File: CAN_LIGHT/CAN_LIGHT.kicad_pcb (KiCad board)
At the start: 2 copper layers, 135.5 x 115.4 mm, 93 parts, among them J1 Conn_ARM_SWD_TagConnect_TC2030

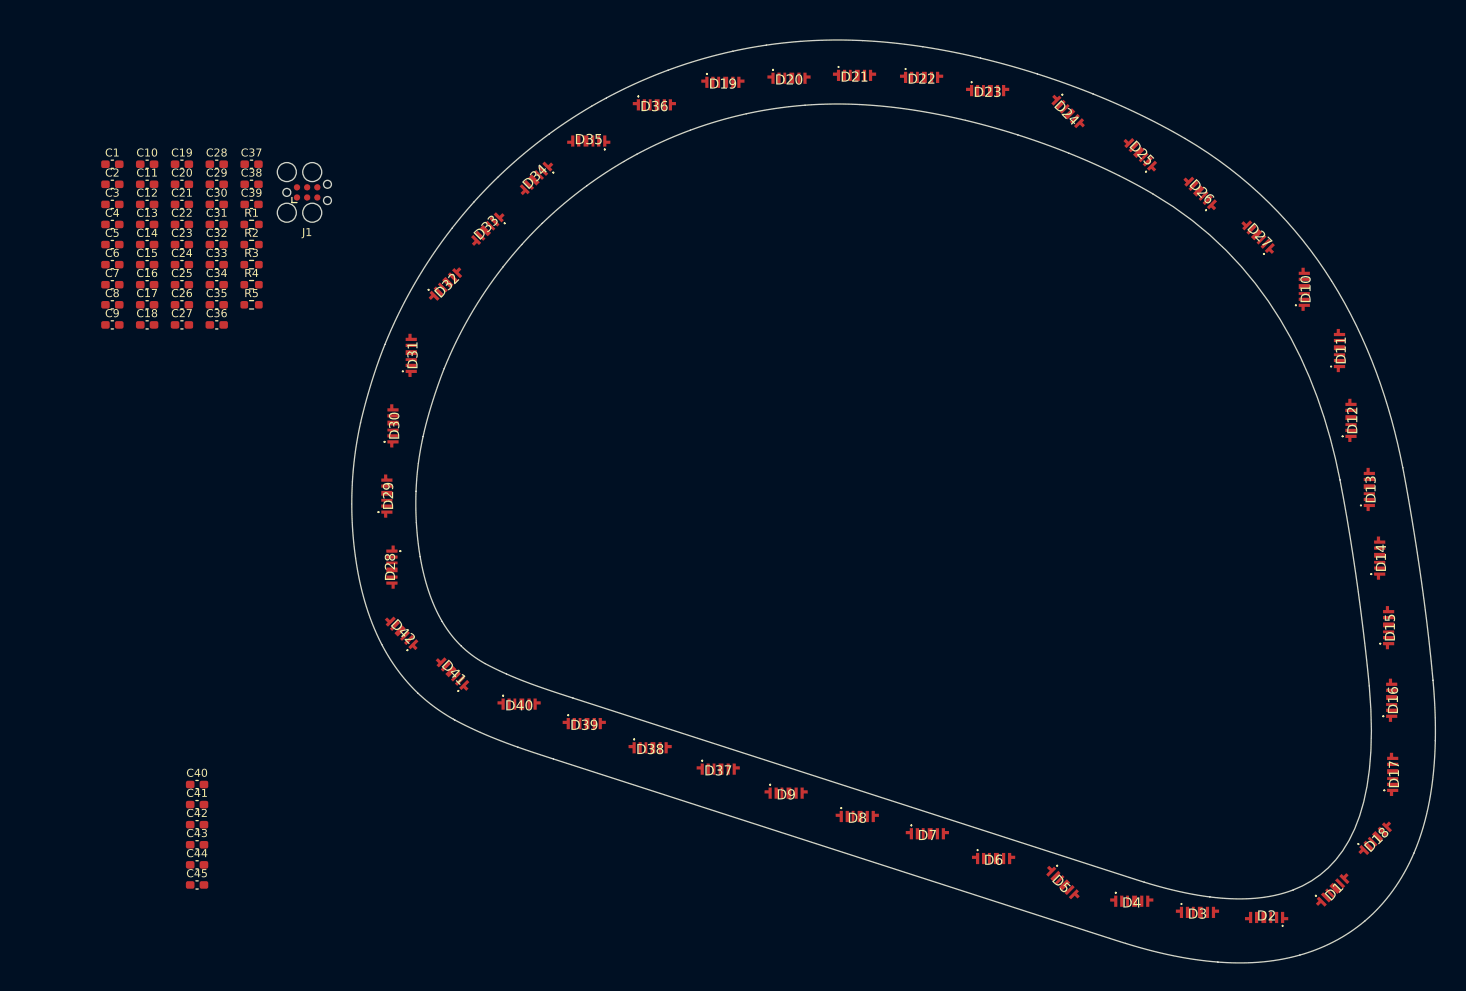
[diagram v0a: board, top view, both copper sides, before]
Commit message: Place more LEDs and experiment with routing paths
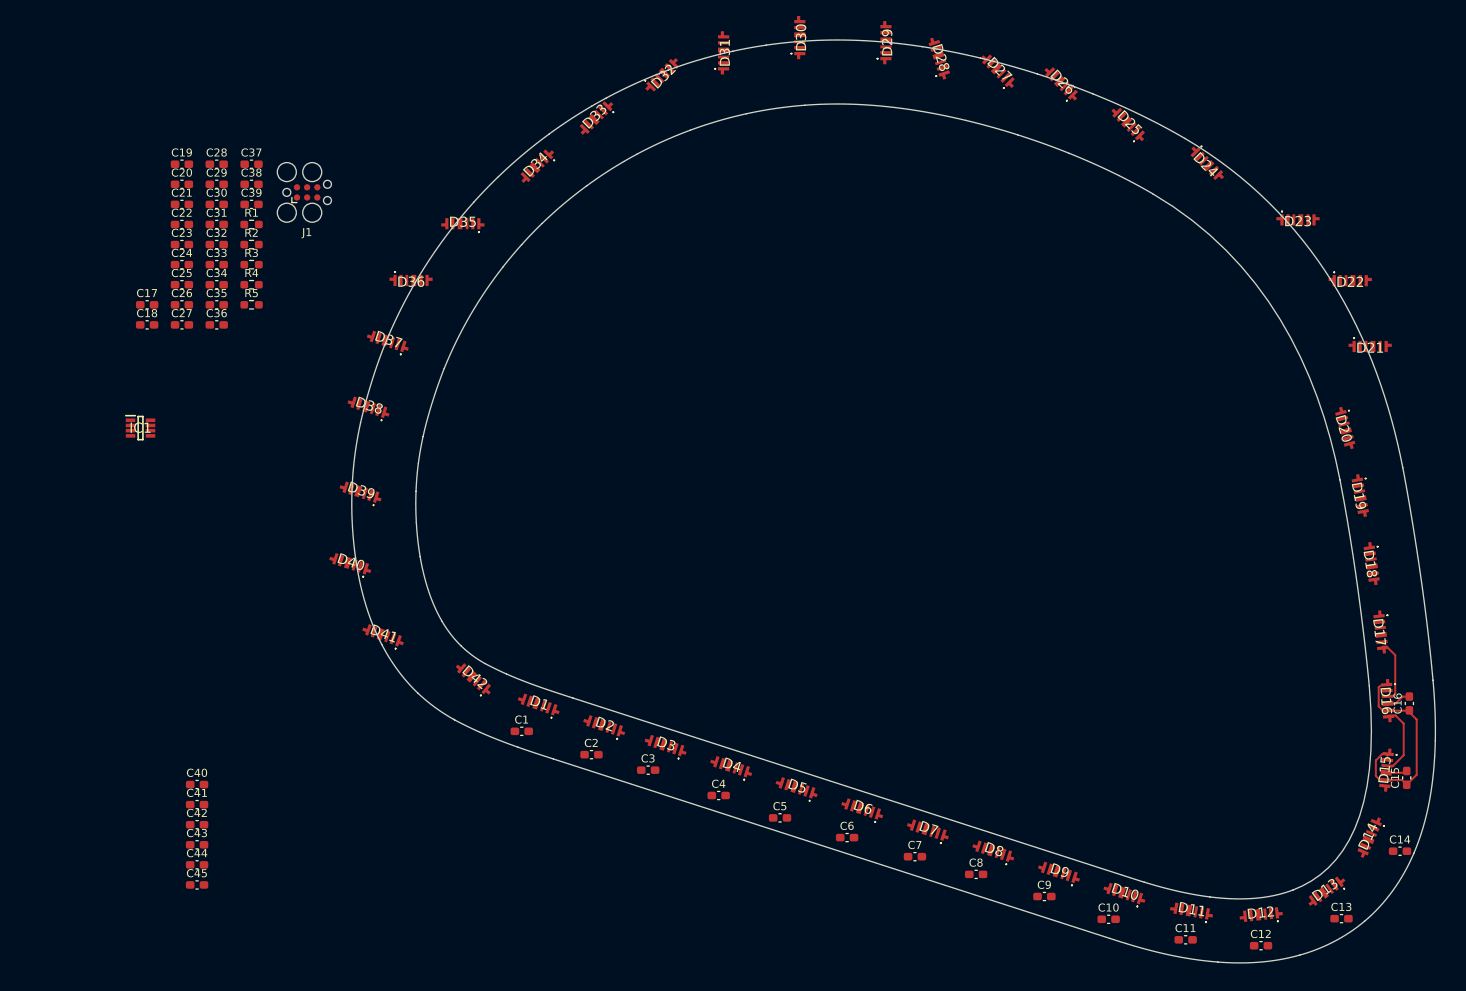
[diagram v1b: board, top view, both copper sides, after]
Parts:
- added IC1: MSPM0C1103SDDFR, MSPM0C1103SDDFR:SOT65P280X110-8N, F.Cu at (39.6, 76.2)
- C1: value 10uF -> 0.1uF
- C3: value 10nF -> 0.1uF
- C43: value 0.1uF -> 10uF
- C45: value 0.1uF -> 10nF
- R4: value 301K -> 169K
- R5: value 169K -> 301K
- moved C14 174.0 mm to (197.0, 129.1)
- moved C13 172.7 mm to (189.7, 137.6)
- moved C15 170.0 mm to (197.8, 120.0), turned to 90 degrees
- moved C12 167.3 mm to (179.6, 140.9)
- moved C16 166.2 mm to (198.2, 110.7), turned to 90 degrees
- moved C11 160.5 mm to (170.2, 140.2)
- moved C10 152.8 mm to (160.6, 137.6)
- moved C9 136.7 mm to (152.6, 134.8)
- moved C8 129.3 mm to (144.0, 132.0)
- moved C7 123.2 mm to (136.4, 129.8)
- moved C6 116.5 mm to (127.9, 127.4)
- moved C5 110.0 mm to (119.5, 125.0)
- moved C4 104.1 mm to (111.8, 122.2)
- moved D1 102.2 mm to (89.5, 110.5), turned to 161 degrees
- moved C3 97.4 mm to (103.0, 119.0)
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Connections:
- C1 pad 1: +3.3V -> +5V
- C2 pad 1: +3.3V -> +5V
- C3 pad 1: Net-(IC1-PA1_/_NRST) -> +5V
- C43 pad 1: +5V -> +3.3V
- C44 pad 1: +5V -> +3.3V
- C45 pad 1: +5V -> Net-(IC1-PA1_/_NRST)
- D11 pad 6: Net-(D11-DIN) -> Net-(D10-DOUT)
- D20 pad 6: Net-(D20-DIN) -> Net-(D19-DOUT)
- D21 pad 6: Net-(D21-DIN) -> Net-(D20-DOUT)
- D22 pad 6: Net-(D19-DOUT) -> Net-(D21-DOUT)
- D23 pad 6: Net-(D20-DOUT) -> Net-(D22-DOUT)
- D24 pad 6: Net-(D21-DOUT) -> Net-(D23-DOUT)
- D25 pad 6: Net-(D22-DOUT) -> Net-(D24-DOUT)
- D26 pad 6: Net-(D23-DOUT) -> Net-(D25-DOUT)
- D27 pad 6: Net-(D24-DOUT) -> Net-(D26-DOUT)
- D28 pad 6: Net-(D25-DOUT) -> Net-(D27-DOUT)
- D29 pad 6: Net-(D26-DOUT) -> Net-(D28-DOUT)
- D30 pad 6: Net-(D27-DOUT) -> Net-(D29-DOUT)
- D31 pad 6: Net-(D28-DOUT) -> Net-(D30-DOUT)
- D32 pad 6: Net-(D29-DOUT) -> Net-(D31-DOUT)
- D33 pad 6: Net-(D30-DOUT) -> Net-(D32-DOUT)
- D34 pad 3: Net-(D20-DIN) -> Net-(D34-DOUT)
- D34 pad 6: Net-(D31-DOUT) -> Net-(D33-DOUT)
- D35 pad 3: Net-(D21-DIN) -> Net-(D35-DOUT)
- D35 pad 6: Net-(D32-DOUT) -> Net-(D34-DOUT)
- D36 pad 6: Net-(D33-DOUT) -> Net-(D35-DOUT)
- D5 pad 6: Net-(D10-DOUT) -> Net-(D4-DOUT)
- D8 pad 3: Net-(D11-DIN) -> Net-(D8-DOUT)
- D9 pad 6: Net-(D4-DOUT) -> Net-(D8-DOUT)
- R4 pad 2: +3.3V -> GND
- R5 pad 2: GND -> +3.3V
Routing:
- net +5V: track 0.00 -> 24.9 mm
- net Net-(D15-DOUT): track 0.00 -> 8.89 mm
- net Net-(D16-DOUT): track 0.00 -> 8.00 mm
- net GND: track 0.00 -> 5.71 mm

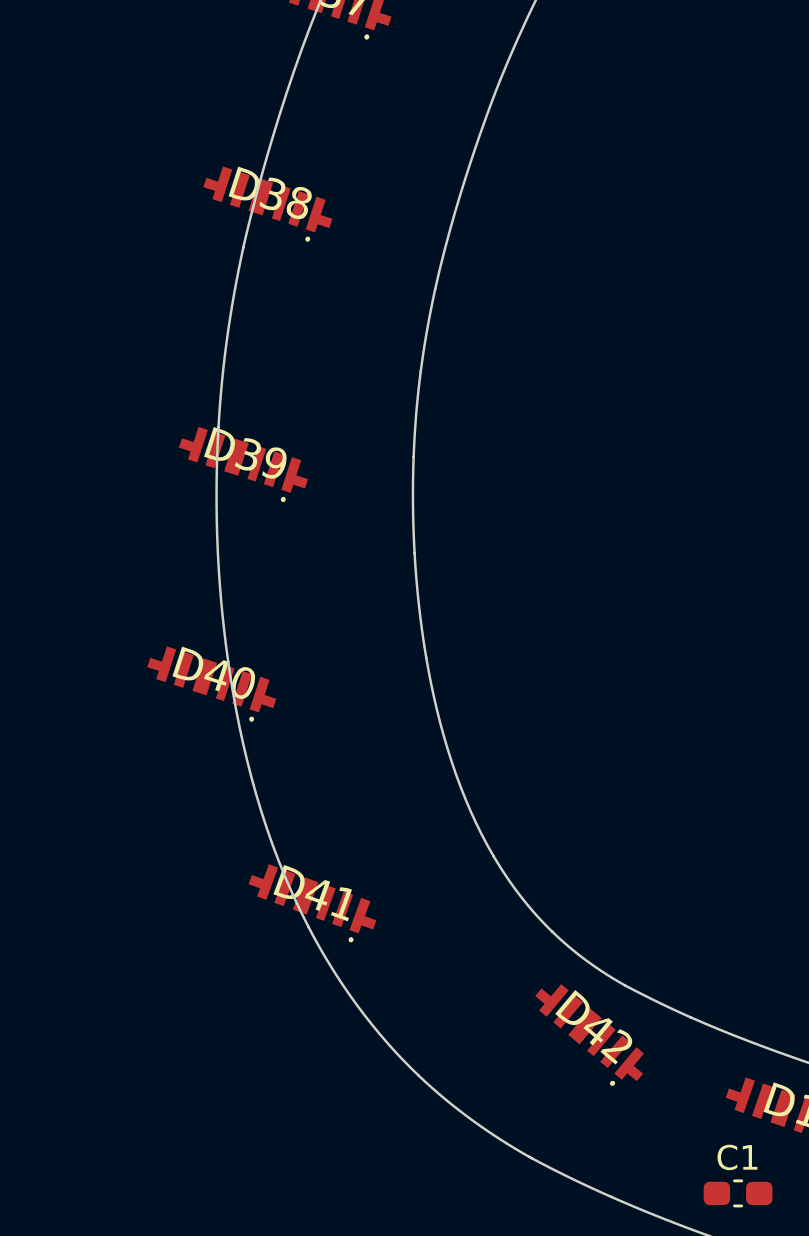
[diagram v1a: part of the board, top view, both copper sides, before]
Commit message: Place more LEDs
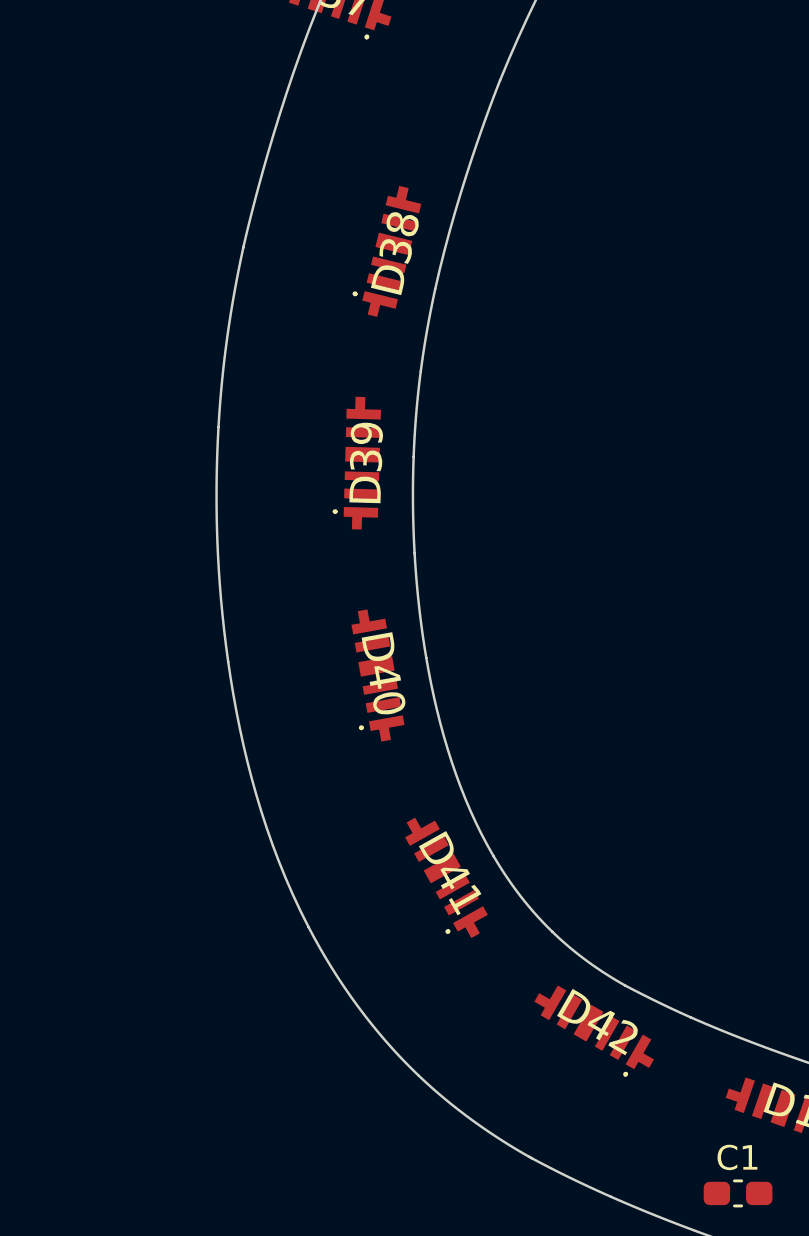
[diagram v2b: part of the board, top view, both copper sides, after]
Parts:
- moved D40 6.93 mm to (72.8, 93.0), turned to 100.25 degrees
- moved D38 5.77 mm to (73.4, 75.9), turned to 76.25 degrees
- moved D41 5.62 mm to (75.6, 101.1), turned to 119.25 degrees
- moved D39 5.02 mm to (72.2, 84.4), turned to 88.4 degrees
- moved D42 0.26 mm to (81.6, 107.1), turned to 150 degrees

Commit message: Finish LED placements
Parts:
- moved C17 163.3 mm to (198.7, 101.1)
- moved C18 159.9 mm to (197.6, 92.6)
- moved C19 157.0 mm to (196.5, 83.6)
- moved C20 153.4 mm to (195.4, 74.8)
- moved C21 148.9 mm to (192.6, 66.2)
- moved C22 143.0 mm to (187.6, 57.8)
- moved C23 136.5 mm to (181.3, 50.5)
- moved C24 130.2 mm to (174.5, 44.5)
- moved C25 122.9 mm to (166.1, 39.1)
- moved C26 115.6 mm to (157.7, 36.0)
- moved C27 108.9 mm to (149.4, 33.0)
- moved C28 91.9 mm to (140.2, 31.0)
- moved C29 83.5 mm to (131.1, 30.0)
- moved C30 74.6 mm to (121.3, 29.5)
- moved C31 65.1 mm to (111.4, 31.9)
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
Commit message: Place caps
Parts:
- moved C20 2.76 mm to (192.8, 75.7), turned to 105.75 degrees
- moved C21 2.75 mm to (190.0, 67.1), turned to 113.5 degrees
- moved C25 2.10 mm to (165.9, 41.1), turned to 152.5 degrees
- moved C34 2.06 mm to (88.9, 44.7), turned to -139.75 degrees
- moved C22 1.97 mm to (185.9, 58.9), turned to 122.75 degrees
- moved C19 1.97 mm to (194.8, 84.6), turned to 100.5 degrees
- moved C30 1.86 mm to (121.9, 31.2), turned to -175.5 degrees
- moved C35 1.83 mm to (82.8, 51.1), turned to -130.75 degrees
- moved C24 1.82 mm to (173.5, 46.0), turned to 143.5 degrees
- moved C36 1.81 mm to (77.2, 58.4), turned to -121.5 degrees
- moved C29 1.69 mm to (132.3, 31.2), turned to 175.5 degrees
- moved C5 1.65 mm to (120.1, 123.4), turned to -18 degrees
- moved C1 1.62 mm to (88.4, 113.0), turned to -19 degrees
- moved C23 1.58 mm to (180.1, 51.6), turned to 133 degrees
- moved C28 1.57 mm to (140.7, 32.5), turned to 168.6 degrees
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
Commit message: Mess with routing
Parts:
- moved C2 1.26 mm to (95.6, 115.4)
- moved C1 1.11 mm to (87.3, 112.7)
- moved C42 0.86 mm to (79.0, 108.8)
- moved C3 0.51 mm to (103.2, 117.8)
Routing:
- net +5V: track 24.9 -> 36.0 mm
- net GND: track 5.71 -> 16.6 mm
- net Net-(D1-DOUT): track 0.00 -> 8.23 mm
- net Net-(D2-DOUT): track 0.00 -> 7.06 mm
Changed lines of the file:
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@@
   )
   (footprint "Capacitor_SMD:C_0603_1608Metric_Pad1.08x0.95mm_HandSolder" (layer "F.Cu")
-    (at 96.774 115.824 -18)
+    (at 95.572714 115.430473 -18)
     (descr "Capacitor SMD 0603 (1608 Metric), square (rectangular) end terminal, IPC_7351 nominal with elongated pad for handsoldering. (Body size source: IPC-SM-782 page 76, https://www.pcb-3d.com/wordpress/wp-content/uploads/ipc-sm-782a_amendment_1_and_2.pdf), generated with kicad-footprint-generator")
     (tags "capacitor handsolder")
@@
   )
   (footprint "Capacitor_SMD:C_0603_1608Metric_Pad1.08x0.95mm_HandSolder" (layer "F.Cu")
-    (at 79.756 109.22 -30)
+    (at 79.009053 108.78875 -30)
     (descr "Capacitor SMD 0603 (1608 Metric), square (rectangular) end terminal, IPC_7351 nominal with elongated pad for handsoldering. (Body size source: IPC-SM-782 page 76, https://www.pcb-3d.com/wordpress/wp-content/uploads/ipc-sm-782a_amendment_1_and_2.pdf), generated with kicad-footprint-generator")
     (tags "capacitor handsolder")
@@
   )
   (footprint "Capacitor_SMD:C_0603_1608Metric_Pad1.08x0.95mm_HandSolder" (layer "F.Cu")
-    (at 103.632 118.11 -18)
+    (at 103.192714 117.843473 -18)
     (descr "Capacitor SMD 0603 (1608 Metric), square (rectangular) end terminal, IPC_7351 nominal with elongated pad for handsoldering. (Body size source: IPC-SM-782 page 76, https://www.pcb-3d.com/wordpress/wp-content/uploads/ipc-sm-782a_amendment_1_and_2.pdf), generated with kicad-footprint-generator")
     (tags "capacitor handsolder")
@@
   )
   (footprint "Capacitor_SMD:C_0603_1608Metric_Pad1.08x0.95mm_HandSolder" (layer "F.Cu")
-    (at 88.392 113.03 -19)
+    (at 87.32249 112.749197 -19)
     (descr "Capacitor SMD 0603 (1608 Metric), square (rectangular) end terminal, IPC_7351 nominal with elongated pad for handsoldering. (Body size source: IPC-SM-782 page 76, https://www.pcb-3d.com/wordpress/wp-content/uploads/ipc-sm-782a_amendment_1_and_2.pdf), generated with kicad-footprint-generator")
     (tags "capacitor handsolder")
@@
   (gr_curve (pts (xy 93.6303 109.9898) (xy 90.8143 109.0833) (xy 87.9942 108.1676) (xy 85.285899 106.9696))
     (stroke (width 0.1) (type solid)) (layer "Edge.Cuts"))
+  (segment (start 97.028 113.568986) (end 97.028 115.062) (width 0.25) (layer "F.Cu") (net 2))
+  (segment (start 87.884 112.776) (end 88.138 113.03) (width 0.25) (layer "F.Cu") (net 2))
+  (segment (start 87.884 112.014) (end 87.884 112.776) (width 0.25) (layer "F.Cu") (net 2))
+  (segment (start 104.908225 115.821761) (end 104.394 116.335986) (width 0.25) (layer "F.Cu") (net 2))
+  (segment (start 104.394 116.335986) (end 104.394 117.729) (width 0.25) (layer "F.Cu") (net 2))
   (segment (start 198.171067 109.806133) (end 197.330667 109.806133) (width 0.25) (layer "F.Cu") (net 2))
   (segment (start 195.282972 119.327641) (end 197.615758 119.327641) (width 0.25) (layer "F.Cu") (net 2))
+  (segment (start 81.131691 107.2062) (end 79.756 108.581891) (width 0.25) (layer "F.Cu") (net 2))
   (segment (start 197.615758 119.327641) (end 197.8406 119.102799) (width 0.25) (layer "F.Cu") (net 2))
   (segment (start 197.330667 109.806133) (end 196.468167 110.668633) (width 0.25) (layer "F.Cu") (net 2))
+  (segment (start 97.237425 113.359561) (end 97.028 113.568986) (width 0.25) (layer "F.Cu") (net 2))
   (segment (start 196.468167 110.668633) (end 195.469007 110.668633) (width 0.25) (layer "F.Cu") (net 2))
+  (segment (start 89.055598 110.685107) (end 89.055598 110.842402) (width 0.25) (layer "F.Cu") (net 2))
+  (segment (start 89.055598 110.842402) (end 87.884 112.014) (width 0.25) (layer "F.Cu") (net 2))
+  (segment (start 104.394 117.729) (end 104.013 118.11) (width 0.25) (layer "F.Cu") (net 2))
+  (segment (start 97.028 115.062) (end 96.393 115.697) (width 0.25) (layer "F.Cu") (net 2))
+  (segment (start 79.756 108.581891) (end 79.756 109.22) (width 0.25) (layer "F.Cu") (net 2))
   (segment (start 194.335426 108.661174) (end 194.335426 111.017225) (width 0.25) (layer "F.Cu") (net 4))
   (segment (start 195.244306 116.990515) (end 195.406986 117.153195) (width 0.25) (layer "F.Cu") (net 4))
+  (segment (start 96.381474 113.081446) (end 96.381474 113.5349) (width 0.25) (layer "F.Cu") (net 4))
+  (segment (start 104.052274 115.8971) (end 102.372428 117.576946) (width 0.25) (layer "F.Cu") (net 4))
   (segment (start 197.976654 111.566954) (end 195.523951 111.566954) (width 0.25) (layer "F.Cu") (net 4))
   (segment (start 194.335426 111.017225) (end 194.885155 111.566954) (width 0.25) (layer "F.Cu") (net 4))
   (segment (start 193.9798 119.717471) (end 193.9798 117.79987) (width 0.25) (layer "F.Cu") (net 4))
+  (segment (start 88.204631 110.770743) (end 86.50698 112.468394) (width 0.25) (layer "F.Cu") (net 4))
   (segment (start 199.0852 112.6755) (end 197.976654 111.566954) (width 0.25) (layer "F.Cu") (net 4))
   (segment (start 194.545159 108.451441) (end 194.335426 108.661174) (width 0.25) (layer "F.Cu") (net 4))
@@
   (segment (start 195.188896 120.222711) (end 194.48504 120.222711) (width 0.25) (layer "F.Cu") (net 4))
   (segment (start 197.8406 120.827799) (end 199.0852 119.583199) (width 0.25) (layer "F.Cu") (net 4))
+  (segment (start 78.750968 108.3575) (end 78.262106 108.3575) (width 0.25) (layer "F.Cu") (net 4))
+  (segment (start 96.381474 113.5349) (end 94.752428 115.163946) (width 0.25) (layer "F.Cu") (net 4))
+  (segment (start 80.352268 106.7562) (end 78.750968 108.3575) (width 0.25) (layer "F.Cu") (net 4))
+  (segment (start 88.204631 110.392095) (end 88.204631 110.770743) (width 0.25) (layer "F.Cu") (net 4))
   (segment (start 197.8406 120.827799) (end 197.235512 120.222711) (width 0.25) (layer "F.Cu") (net 4))
   (segment (start 193.9798 117.79987) (end 194.789155 116.990515) (width 0.25) (layer "F.Cu") (net 4))
   (segment (start 194.48504 120.222711) (end 193.9798 119.717471) (width 0.25) (layer "F.Cu") (net 4))
   (segment (start 197.235512 120.222711) (end 195.188896 120.222711) (width 0.25) (layer "F.Cu") (net 4))
+  (segment (start 104.052274 115.543646) (end 104.052274 115.8971) (width 0.25) (layer "F.Cu") (net 4))
   (segment (start 199.0852 119.583199) (end 199.0852 112.6755) (width 0.25) (layer "F.Cu") (net 4))
   (segment (start 194.885155 111.566954) (end 195.523951 111.566954) (width 0.25) (layer "F.Cu") (net 4))
   (segment (start 194.789155 116.990515) (end 195.244306 116.990515) (width 0.25) (layer "F.Cu") (net 4))
+  (segment (start 94.869 113.648865) (end 95.072115 113.44575) (width 0.25) (layer "F.Cu") (net 13))
+  (segment (start 95.072115 113.44575) (end 95.504436 113.44575) (width 0.25) (layer "F.Cu") (net 13))
+  (segment (start 89.535 111.887) (end 91.567 113.919) (width 0.25) (layer "F.Cu") (net 13))
+  (segment (start 91.567 113.919) (end 94.869 113.919) (width 0.25) (layer "F.Cu") (net 13))
+  (segment (start 94.869 113.919) (end 94.869 113.648865) (width 0.25) (layer "F.Cu") (net 13))
+  (segment (start 89.882927 110.969979) (end 89.882927 111.539073) (width 0.25) (layer "F.Cu") (net 13))
+  (segment (start 89.882927 111.539073) (end 89.535 111.887) (width 0.25) (layer "F.Cu") (net 13))
+  (segment (start 98.0696 113.629951) (end 97.917 113.782551) (width 0.25) (layer "F.Cu") (net 15))
+  (segment (start 97.917 114.681) (end 99.441 116.205) (width 0.25) (layer "F.Cu") (net 15))
+  (segment (start 97.917 113.782551) (end 97.917 114.681) (width 0.25) (layer "F.Cu") (net 15))
+  (segment (start 99.441 116.205) (end 102.8065 116.205) (width 0.25) (layer "F.Cu") (net 15))
+  (segment (start 102.8065 116.205) (end 103.10355 115.90795) (width 0.25) (layer "F.Cu") (net 15))
   (segment (start 197.4596 117.133976) (end 197.4596 113.1824) (width 0.25) (layer "F.Cu") (net 40))
   (segment (start 197.4596 113.1824) (end 196.446015 112.168815) (width 0.25) (layer "F.Cu") (net 40))
